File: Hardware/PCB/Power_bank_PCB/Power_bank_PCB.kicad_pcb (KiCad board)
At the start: 2 copper layers, 69.5 x 36.3 mm, 96 parts, among them IC1 TPS63070RNMR, IC2 TPS63070RNMR, J1 Alterative_charging, J2 Vout, Q1 2N7002, Q2 8205A, Q3 2N7002, Q4 2N7002, Q5 2N7002, Q6 DMP3099L, U1 TP4056-42-ESOP8, U2 MCP4018-10k, U3 DW01A, U4 TPS61022, U5 STM32U031F8Px, U6 INA219AxD

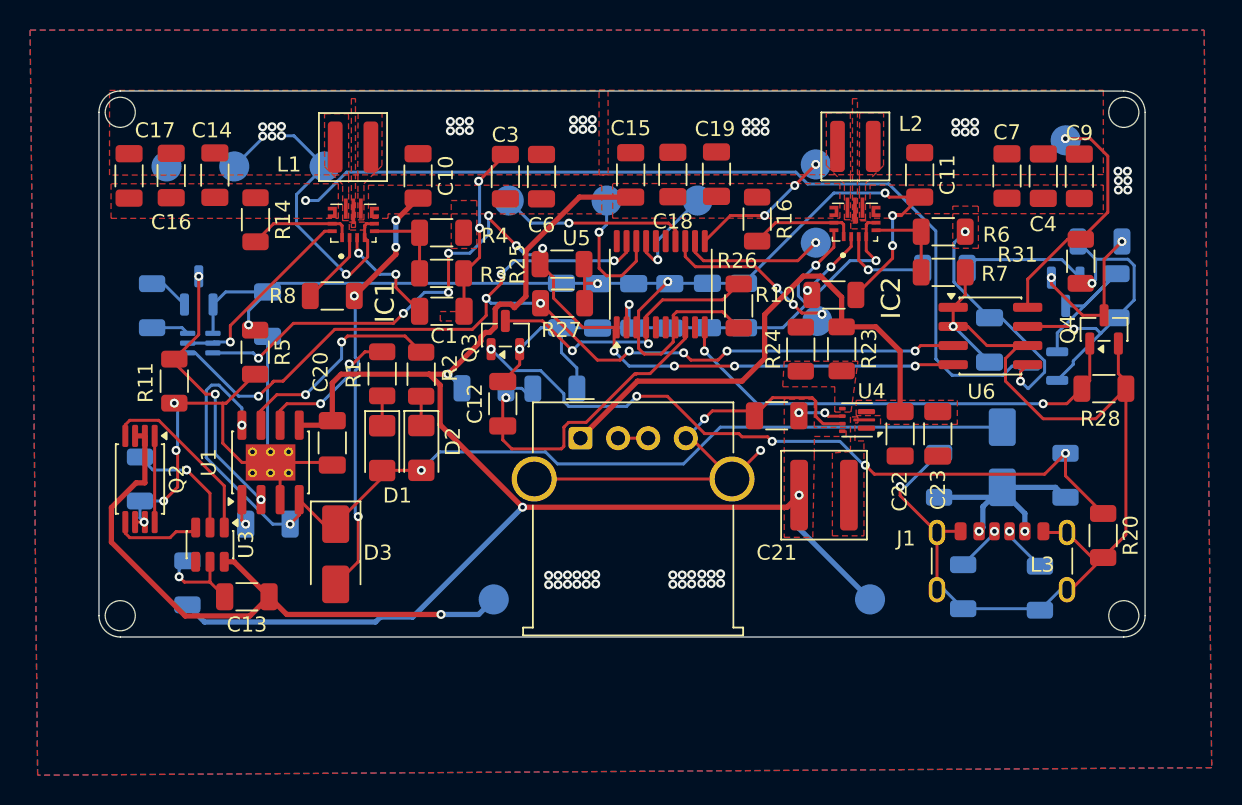
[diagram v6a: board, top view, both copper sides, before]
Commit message: Added missing SLT files and added logos
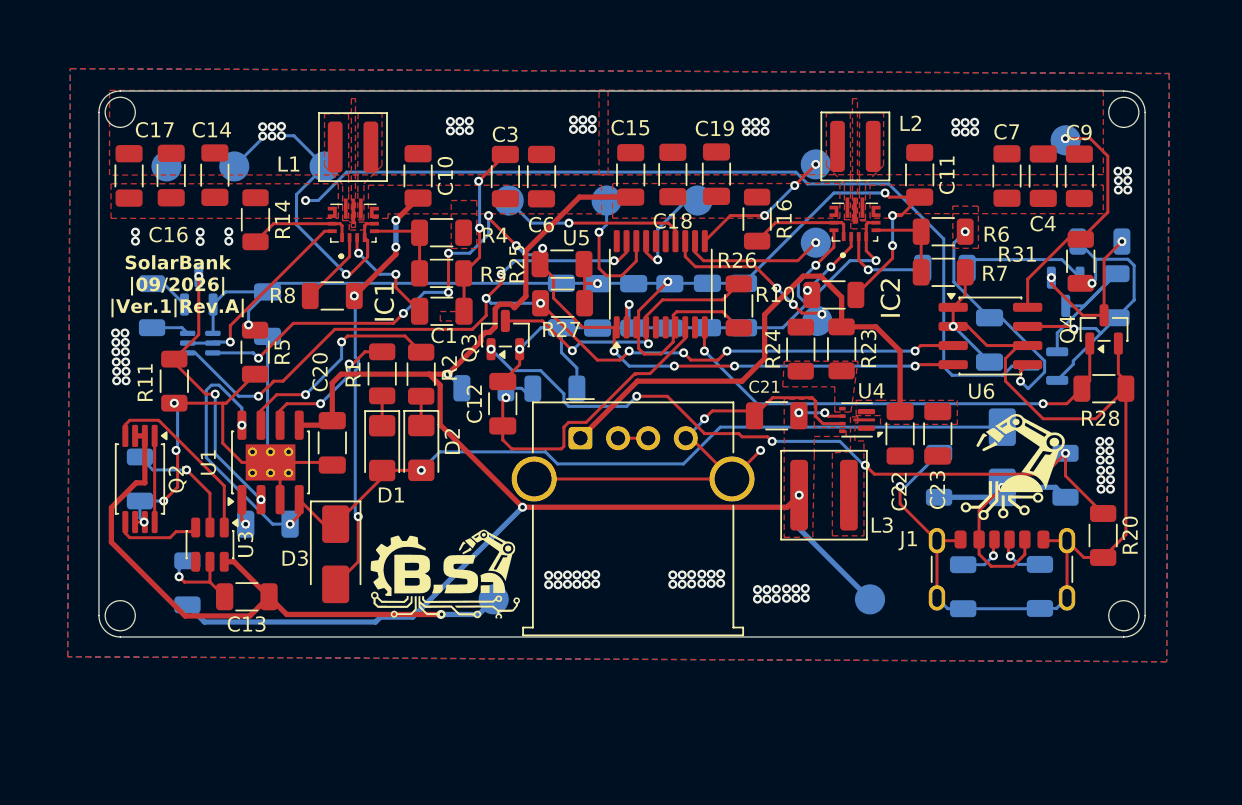
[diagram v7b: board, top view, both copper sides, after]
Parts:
- added G***: LOGO, Logo_footprint:Logo_7_7, F.Cu at (126.5, 60.7)
- added G***: LOGO, Logo_footprint:Logo_10_6, F.Cu at (88.8, 67.8)
- added G***: LOGO, Logo_footprint:Logo_15_15, B.Cu at (85.8, 54.3)
- L1, L2: value 1.5uH / XFL4020 -> 1.5uH / XFL4020-152MEC
- moved J1 0.55 mm to (125.8, 68.6)
- moved R18 0.12 mm to (128.3, 68.6)
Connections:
- IC1 pad 16: Vfoto -> (no net)
- IC1 pad 17: Vcharge -> (no net)
- IC2 pad 16: Vbat -> (no net)
- IC2 pad 17: +3.3V -> (no net)
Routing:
- net Net-(D4-A): track 16.0 -> 19.0 mm, vias 2 -> 1
- net GND: track 245.7 -> 246.8 mm, vias 77 -> 119
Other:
- board text added: "3x GND"
- board text added: "Battery+"
- board text added: "Battery-"
- board text added: "Button"
- board text added: "FotoPanel+"
- board text added: "Green Led"
- board text added: "RedLed"
- board text added: "SWCLK"
- board text added: "SWDIO"
- board text added: "SolarBank |09/2026| |Ver.1|Rev.A|"
- board text added: "Yellow Led"
- board text added: "|Use Li-pol/Li-ion cells| |Fotopanel input voltage: 2-16 V|"
